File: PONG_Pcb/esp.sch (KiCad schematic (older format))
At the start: 17 parts, among them J8 ESP_Conn, J9 ESP_Prog_Conn, Q1 BSS138, Q2 BSS138, SW2 SW_Push, SW3 SW_Push_SPDT, SW4 SW_Push_SPDT, SW6 SW_Push_SPDT

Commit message: Drobne poprawki
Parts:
- removed SW6: SW_Push_SPDT, LIB_PONG_Display:SPDT_switch, symbol Switch:SW_Push_SPDT
- added D5: GREEN_LED, Diode_SMD:D_0805_2012Metric_Pad1.15x1.40mm_HandSolder, symbol Device:LED
- added R15: 5R1, Resistor_SMD:R_0603_1608Metric_Pad1.05x0.95mm_HandSolder, symbol Device:R
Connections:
- net +3V3: now also J9.1 (Pin_1)
- net ESP_GPIO2: now also R15.2; no longer R14.2, SW3.1 (A), SW4.1 (A)
- net GND: now also D5.1 (K)
- new net: R14.2, SW3.1 (A), SW4.1 (A)
- new net: D5.2 (A), R15.1
- no-connect marks 1 -> 0
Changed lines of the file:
@@
 L power:+3.3V #PWR062
 U 1 1 5E859CE6
-P 5200 2600
-F 0 "#PWR062" H 5200 2450 50  0001 C CNN
-F 1 "+3.3V" H 5215 2773 50  0000 C CNN
-F 2 "" H 5200 2600 50  0001 C CNN
-F 3 "" H 5200 2600 50  0001 C CNN
-	1    5200 2600
+P 5000 2650
+F 0 "#PWR062" H 5000 2500 50  0001 C CNN
+F 1 "+3.3V" H 5015 2823 50  0000 C CNN
+F 2 "" H 5000 2650 50  0001 C CNN
+F 3 "" H 5000 2650 50  0001 C CNN
+	1    5000 2650
 	1    0    0    -1
 $EndComp
@@
 Text Notes 3500 4650 0    50   ~ 0
 Przycisk resetu układu ESP
-Text HLabel 8350 2300 0    50   Input ~ 0
+Text HLabel 7700 2300 0    50   Input ~ 0
 ESP_GPIO2
 $Comp
@@
 	9600 3400 9600 3650
 Wire Wire Line
-	8350 2300 9300 2300
-Wire Wire Line
-	9300 2300 9300 2700
-Wire Wire Line
 	9300 2700 9100 2700
 Wire Wire Line
@@
 	9300 1900 9300 1800
 Wire Wire Line
-	9300 2200 9300 2300
-Connection ~ 9300 2300
-$Comp
-L Switch:SW_Push_SPDT SW6
-U 1 1 5EAD59E6
-P 4800 2800
-F 0 "SW6" H 4800 3085 50  0000 C CNN
-F 1 "SW_Push_SPDT" H 4800 2994 50  0000 C CNN
-F 2 "LIB_PONG_Display:SPDT_switch" H 4800 2800 50  0001 C CNN
-F 3 "~" H 4800 2800 50  0001 C CNN
-	1    4800 2800
-	1    0    0    -1
-$EndComp
-NoConn ~ 5000 2900
-Wire Wire Line
-	5000 2700 5200 2700
-Wire Wire Line
-	5200 2700 5200 2600
-Wire Wire Line
-	4350 2800 4600 2800
-Wire Wire Line
 	4350 2800 4350 3050
+Wire Wire Line
+	9300 2200 9300 2700
+$Comp
+L Device:LED D5
+U 1 1 5EBDC983
+P 8500 2300
+F 0 "D5" H 8493 2045 50  0000 C CNN
+F 1 "GREEN_LED" H 8493 2136 50  0000 C CNN
+F 2 "Diode_SMD:D_0805_2012Metric_Pad1.15x1.40mm_HandSolder" H 8500 2300 50  0001 C CNN
+F 3 "~" H 8500 2300 50  0001 C CNN
+	1    8500 2300
+	-1   0    0    1
+$EndComp
+$Comp
+L Device:R R15
+U 1 1 5EBE03B1
+P 8000 2300
+F 0 "R15" V 7793 2300 50  0000 C CNN
+F 1 "5R1" V 7884 2300 50  0000 C CNN
+F 2 "Resistor_SMD:R_0603_1608Metric_Pad1.05x0.95mm_HandSolder" V 7930 2300 50  0001 C CNN
+F 3 "~" H 8000 2300 50  0001 C CNN
+	1    8000 2300
+	0    1    1    0
+$EndComp
+$Comp
+L power:GND #PWR0113
+U 1 1 5EBE0F09
+P 8850 2300
+F 0 "#PWR0113" H 8850 2050 50  0001 C CNN
+F 1 "GND" V 8855 2172 50  0000 R CNN
+F 2 "" H 8850 2300 50  0001 C CNN
+F 3 "" H 8850 2300 50  0001 C CNN
+	1    8850 2300
+	0    -1   -1   0
+$EndComp
+Wire Wire Line
+	7700 2300 7850 2300
+Wire Wire Line
+	8150 2300 8350 2300
+Wire Wire Line
+	8650 2300 8850 2300
+Wire Wire Line
+	4350 2800 5000 2800
+Wire Wire Line
+	5000 2650 5000 2800
 $EndSCHEMATC

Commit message: Ostatnia wersja
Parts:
- added TP4, TP5: TestPoint, TestPoint:TestPoint_Loop_D1.80mm_Drill1.0mm_Beaded, symbol Connector:TestPoint
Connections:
- net ESP_RX: now also TP4.1
- net ESP_TX: now also TP5.1
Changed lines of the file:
@@
 	4600 2250 4700 2250
 Wire Wire Line
-	4600 2350 4700 2350
-Wire Wire Line
-	3950 2050 4100 2050
+	4600 2350 5400 2350
+Wire Wire Line
+	3200 2050 3550 2050
 Wire Wire Line
 	3950 2150 4100 2150
@@
 Wire Wire Line
 	4600 2050 4800 2050
-Text Label 4700 2350 0    50   ~ 0
+Text Label 5650 2350 0    50   ~ 0
 ESP_TX
-Text Label 3950 2050 2    50   ~ 0
+Text Label 3200 2050 2    50   ~ 0
 ESP_RX
 Text Label 4350 3250 2    50   ~ 0
@@
 Wire Wire Line
 	5000 2650 5000 2800
+$Comp
+L Connector:TestPoint TP5
+U 1 1 5EC60E71
+P 5400 2100
+F 0 "TP5" H 5458 2218 50  0000 L CNN
+F 1 "TestPoint" H 5458 2127 50  0000 L CNN
+F 2 "TestPoint:TestPoint_Loop_D1.80mm_Drill1.0mm_Beaded" H 5600 2100 50  0001 C CNN
+F 3 "~" H 5600 2100 50  0001 C CNN
+	1    5400 2100
+	1    0    0    -1
+$EndComp
+$Comp
+L Connector:TestPoint TP4
+U 1 1 5EC615EB
+P 3550 1800
+F 0 "TP4" H 3608 1918 50  0000 L CNN
+F 1 "TestPoint" H 3608 1827 50  0000 L CNN
+F 2 "TestPoint:TestPoint_Loop_D1.80mm_Drill1.0mm_Beaded" H 3750 1800 50  0001 C CNN
+F 3 "~" H 3750 1800 50  0001 C CNN
+	1    3550 1800
+	1    0    0    -1
+$EndComp
+Wire Wire Line
+	5400 2100 5400 2350
+Connection ~ 5400 2350
+Wire Wire Line
+	5400 2350 5650 2350
+Wire Wire Line
+	3550 1800 3550 2050
+Connection ~ 3550 2050
+Wire Wire Line
+	3550 2050 4100 2050
 $EndSCHEMATC

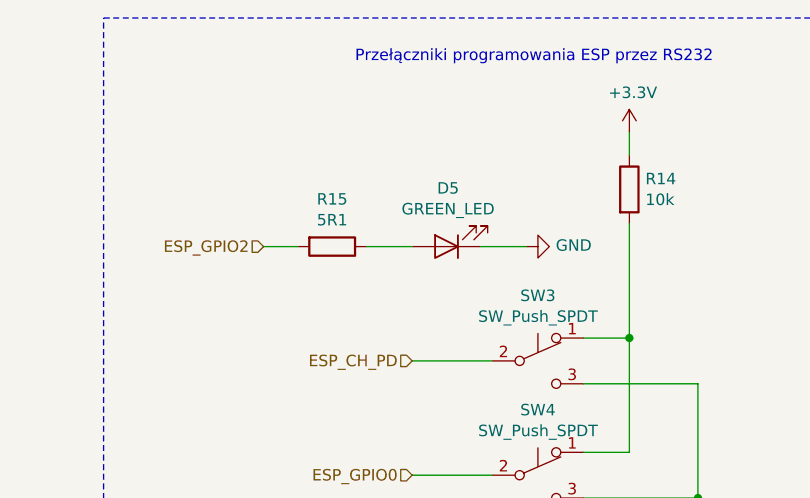
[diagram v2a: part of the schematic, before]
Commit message: Drobna zmiana wartości elementów
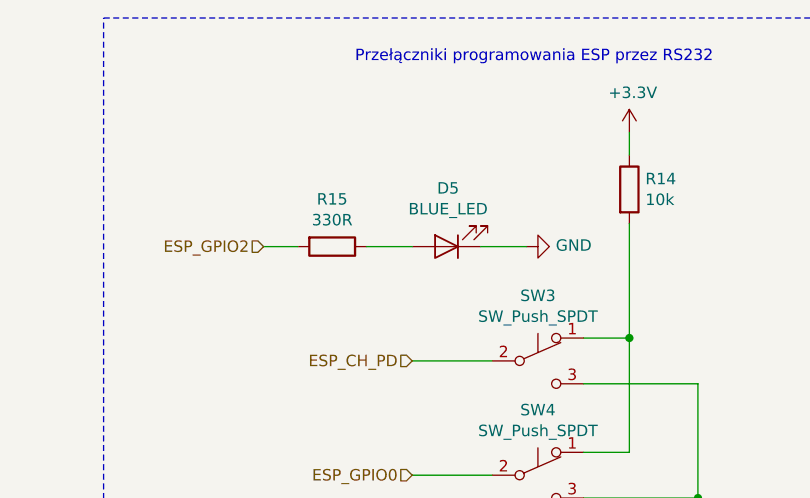
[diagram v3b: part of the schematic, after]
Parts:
- D5: value GREEN_LED -> BLUE_LED
- R15: value 5R1 -> 330R
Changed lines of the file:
@@
 P 8500 2300
 F 0 "D5" H 8493 2045 50  0000 C CNN
-F 1 "GREEN_LED" H 8493 2136 50  0000 C CNN
+F 1 "BLUE_LED" H 8493 2136 50  0000 C CNN
 F 2 "Diode_SMD:D_0805_2012Metric_Pad1.15x1.40mm_HandSolder" H 8500 2300 50  0001 C CNN
 F 3 "~" H 8500 2300 50  0001 C CNN
@@
 P 8000 2300
 F 0 "R15" V 7793 2300 50  0000 C CNN
-F 1 "5R1" V 7884 2300 50  0000 C CNN
+F 1 "330R" V 7884 2300 50  0000 C CNN
 F 2 "Resistor_SMD:R_0603_1608Metric_Pad1.05x0.95mm_HandSolder" V 7930 2300 50  0001 C CNN
 F 3 "~" H 8000 2300 50  0001 C CNN

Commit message: poprawki koncowe
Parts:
- added R1: 10k, Resistor_SMD:R_0603_1608Metric_Pad1.05x0.95mm_HandSolder, symbol Device:R
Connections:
- net +3V3: now also R1.1
- net at R14.2, SW3.1 (A): no longer SW4.1 (A)
- new net: R1.2, SW4.1 (A)
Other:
- note added: "Konwerter stanów logicznych\n"
- note removed: "konwerter stanów logicznych\n"
- moved on the sheet: C22, D4, D5, J8, J9, Q1, Q2, R10, R11, R12, R13, R14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
